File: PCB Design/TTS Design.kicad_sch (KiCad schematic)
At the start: 22 parts, among them J1 Screw_Terminal_01x02, J2 Screw_Terminal_01x02, J3 Screw_Terminal_01x04, J5 Screw_Terminal_01x03, Q1 IRLZ44N, SW1 SW_DPDT_x2, SW2 SW_DPDT_x2, U1 ESP32-DevKitC, U2 Generic_5v_Module

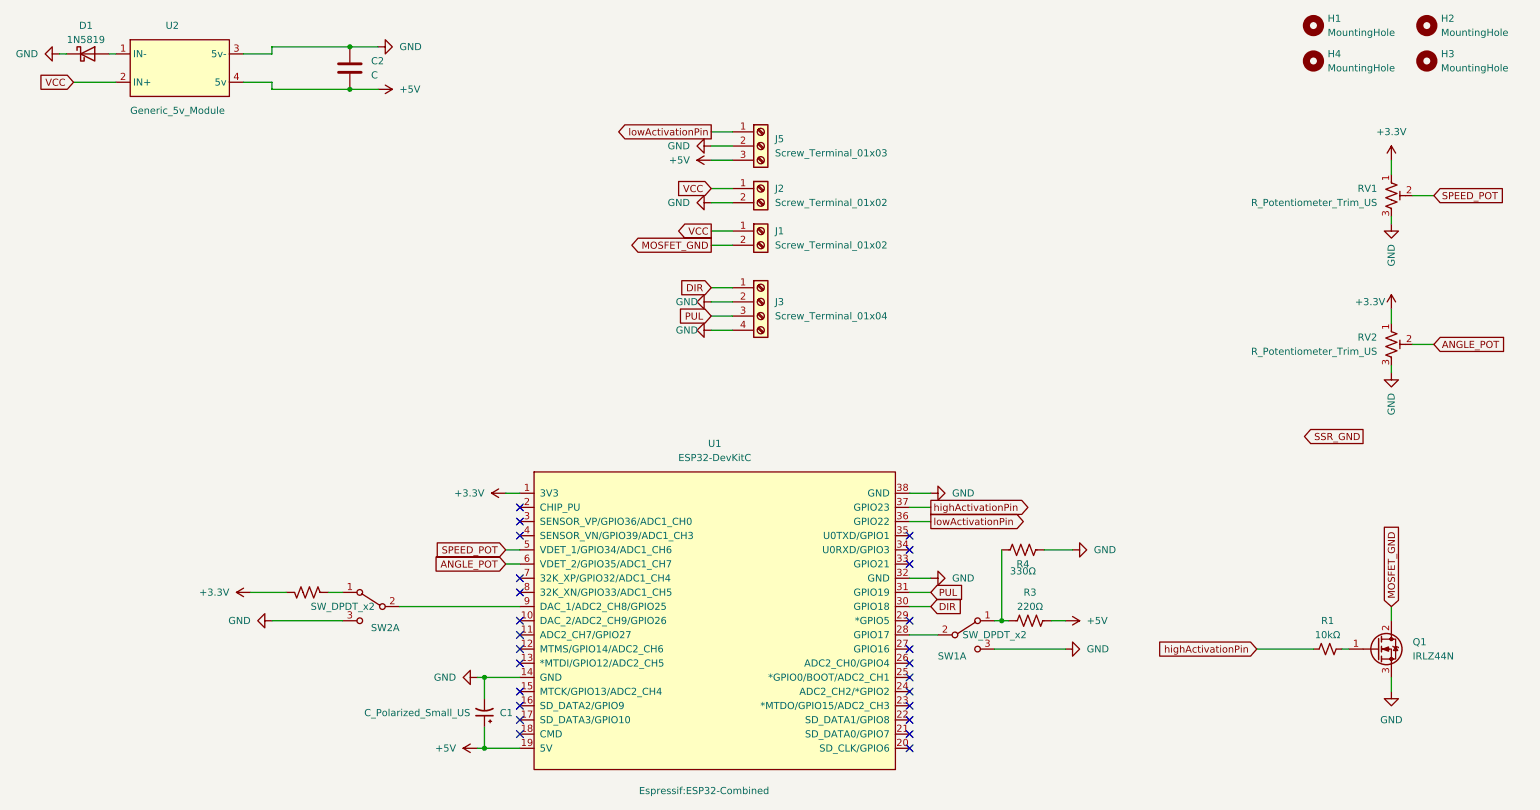
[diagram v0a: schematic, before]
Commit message: PCB changes to integrate stepper motor
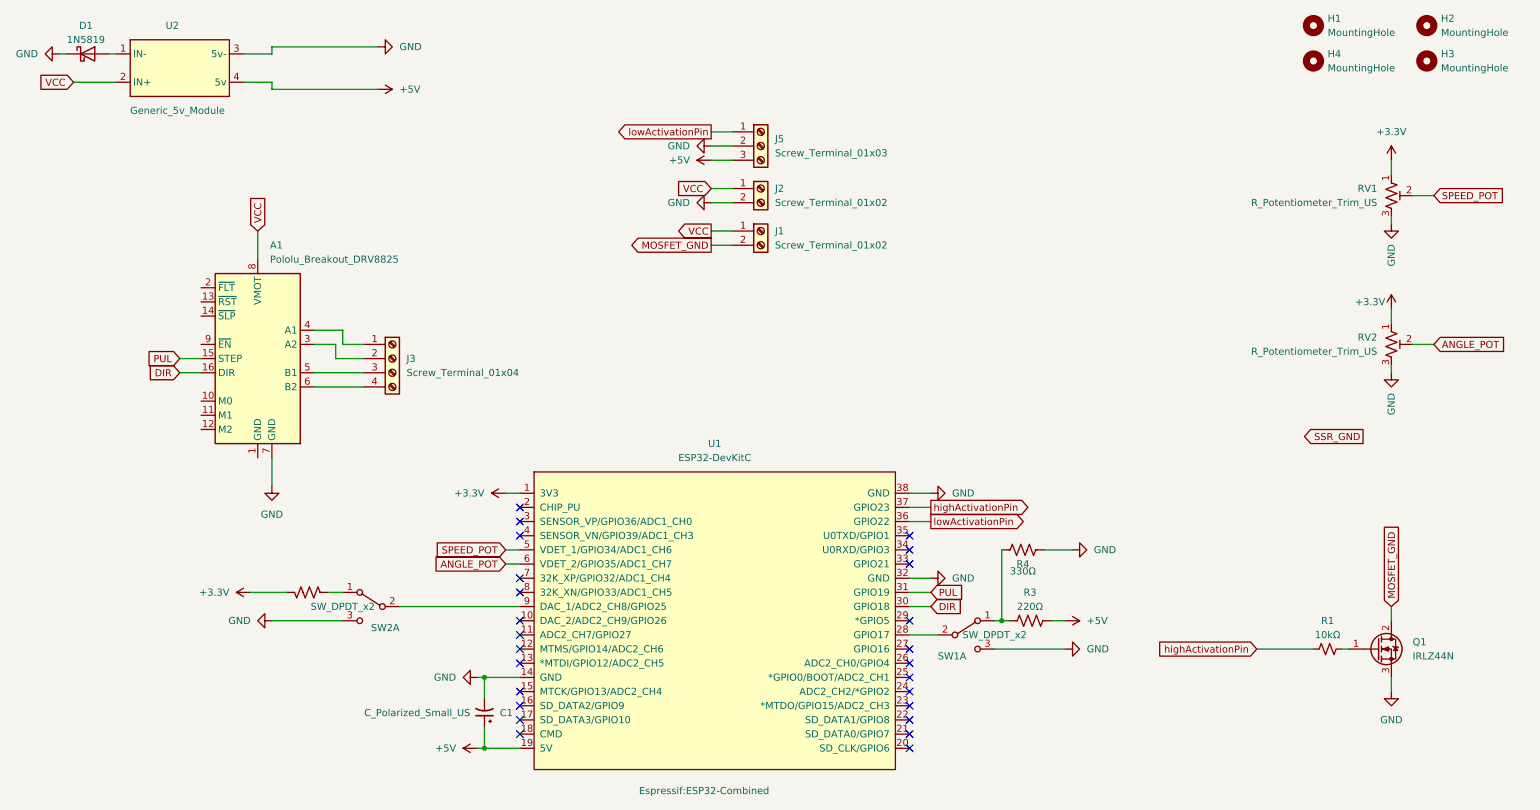
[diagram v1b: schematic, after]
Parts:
- removed C2: C, Capacitor_THT:C_Disc_D3.0mm_W1.6mm_P2.50mm, symbol Device:C
- added A1: Pololu_Breakout_DRV8825, Module:Pololu_Breakout-16_15.2x20.3mm, symbol Driver_Motor:Pololu_Breakout_DRV8825
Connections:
- net DIR: now also A1.16 (DIR); no longer J3.1 (Pin_1)
- net GND: now also A1.7 (GND); no longer J3.2 (Pin_2), J3.4 (Pin_4)
- net PUL: now also A1.15 (STEP); no longer J3.3 (Pin_3)
- net VCC: now also A1.8 (VMOT)
- new net: A1.3 (A2), J3.2 (Pin_2)
- new net: A1.4 (A1), J3.1 (Pin_1)
- new net: A1.5 (B1), J3.3 (Pin_3)
- new net: A1.6 (B2), J3.4 (Pin_4)
